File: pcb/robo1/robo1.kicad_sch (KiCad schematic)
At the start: 9 parts, among them J1 Conn_02x05_Odd_Even, J2 Conn_02x05_Odd_Even, J3 Conn_01x05_Pin, J4 Conn_01x05_Pin, U1 Pico

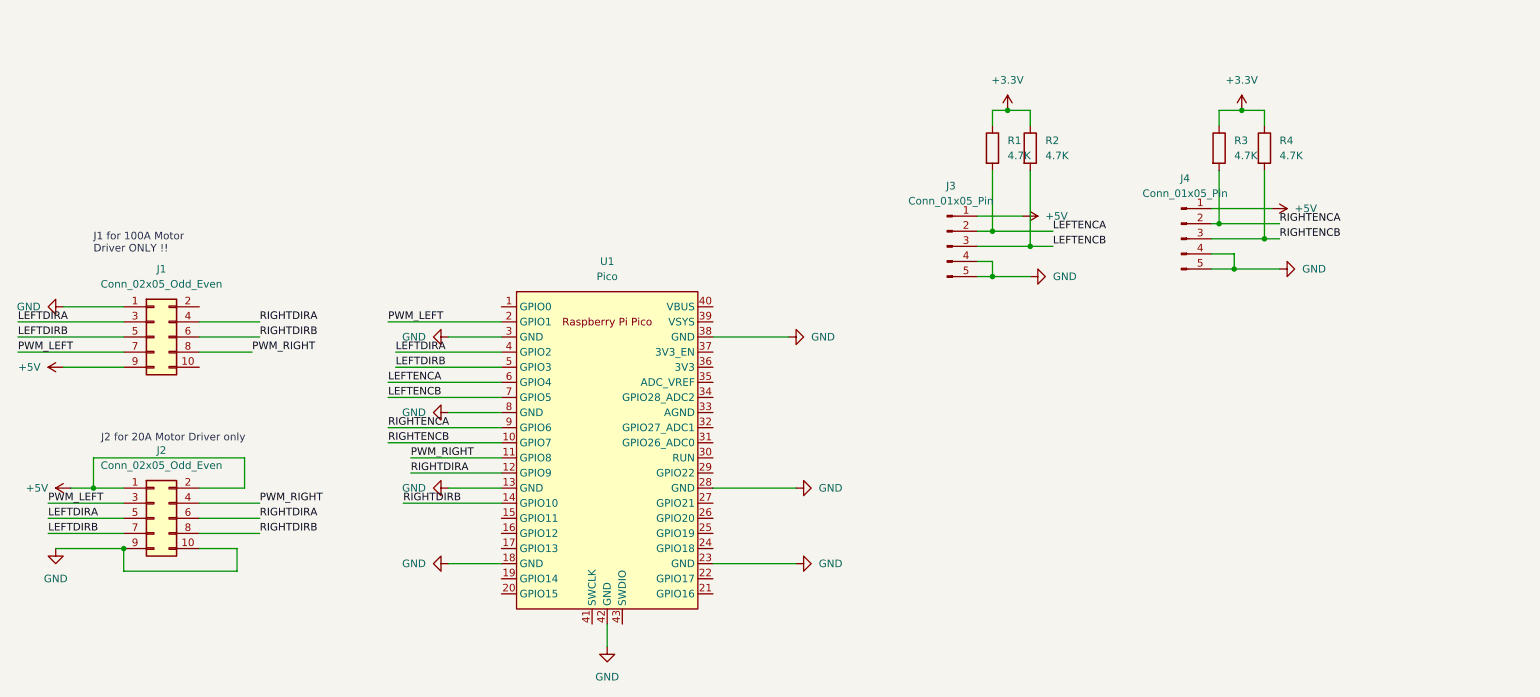
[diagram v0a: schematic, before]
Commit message: Add OLED to PCB
OLED added to pcb
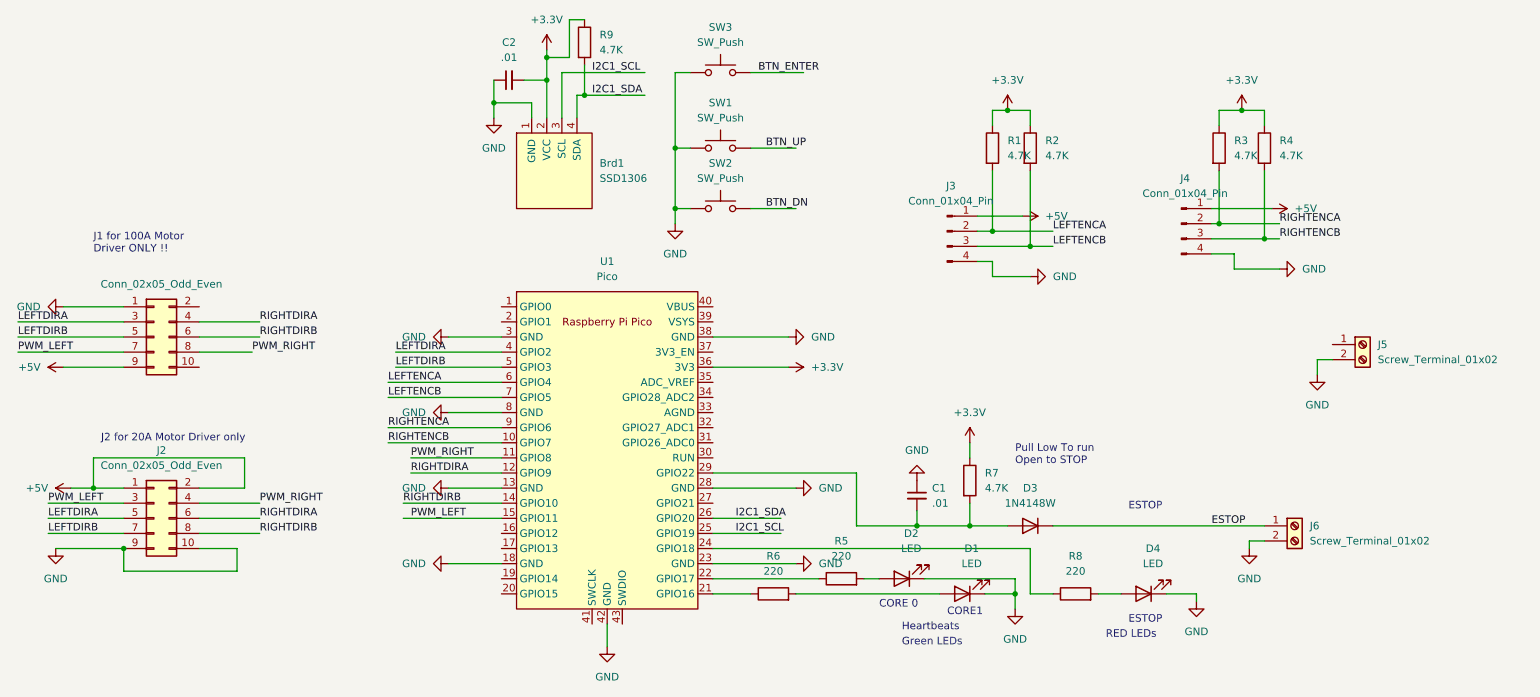
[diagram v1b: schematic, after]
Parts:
- removed J3, J4: Conn_01x05_Pin, Connector_PinHeader_2.54mm:PinHeader_1x05_P2.54mm_Vertical, symbol Connector:Conn_01x05_Pin
- added Brd1: SSD1306, SSD1306:128x64OLED, symbol SSD1306-128x64_OLED:SSD1306
- added C1, C2: .01, Capacitor_SMD:C_0603_1608Metric_Pad1.08x0.95mm_HandSolder, symbol Device:C_Small
- added D1, D2, D4: LED, LED_SMD:LED_1206_3216Metric_Pad1.42x1.75mm_HandSolder, symbol Device:LED
- added D3: 1N4148W, Diode_SMD:D_SOD-123, symbol Diode:1N4148W
- added J3, J4: Conn_01x04_Pin, Connector_PinHeader_2.54mm:PinHeader_1x04_P2.54mm_Vertical, symbol Connector:Conn_01x04_Pin
- added J5, J6: Screw_Terminal_01x02, TerminalBlock:TerminalBlock_bornier-2_P5.08mm, symbol Connector:Screw_Terminal_01x02
- added R5, R6, R8: 220, Resistor_SMD:R_0201_0603Metric_Pad0.64x0.40mm_HandSolder, symbol Device:R
- added R7, R9: 4.7K, Resistor_SMD:R_0201_0603Metric_Pad0.64x0.40mm_HandSolder, symbol Device:R
- added SW1, SW2, SW3: SW_Push, Button_Switch_THT:SW_PUSH_6mm, symbol Switch:SW_Push
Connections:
- net +3.3V: now also U1.36 (3V3), Brd1.2 (VCC), C2.2, R7.1, R9.1
- net +5V: now also J3.1 (Pin_1), J4.1 (Pin_1)
- net GND: now also Brd1.1 (GND), C1.1, C2.1, D1.1 (K), D2.1 (K), D4.1 (K), J3.4 (Pin_4), J4.4 (Pin_4), J5.2 (Pin_2), J6.2 (Pin_2), SW1.1, SW2.1, SW3.1
- net LEFTENCA: now also J3.2 (Pin_2)
- net LEFTENCB: now also J3.3 (Pin_3)
- net PWM_LEFT: now also U1.15 (GPIO11); no longer U1.2 (GPIO1)
- net RIGHTENCA: now also J4.2 (Pin_2)
- net RIGHTENCB: now also J4.3 (Pin_3)
- net at U1.21 (GPIO16): now also R6.1
- net at U1.22 (GPIO17): now also R5.1
- net at U1.24 (GPIO18): now also R8.1
- net I2C1_SCL: now reaches U1.25 (GPIO19)
- net I2C1_SCL: now also Brd1.3 (SCL)
- net I2C1_SDA: now reaches U1.26 (GPIO20)
- net I2C1_SDA: now also Brd1.4 (SDA), R9.2
- net at U1.29 (GPIO22): now also C1.2, D3.2 (A), R7.2
- new net: D4.2 (A), R8.2
- new net: D2.2 (A), R5.2
- new net: D1.2 (A), R6.2
- new net BTN_DN: SW2.2
- new net BTN_ENTER: SW3.2
- new net BTN_UP: SW1.2
- new net ESTOP: D3.1 (K), J6.1 (Pin_1)
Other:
- note added: "CORE 0"
- note added: "CORE1"
- note added: "ESTOP"
- note added: "Green LEDs"
- note added: "Heartbeats"
- note added: "Pull Low To run Open to STOP"
- note added: "RED LEDs"

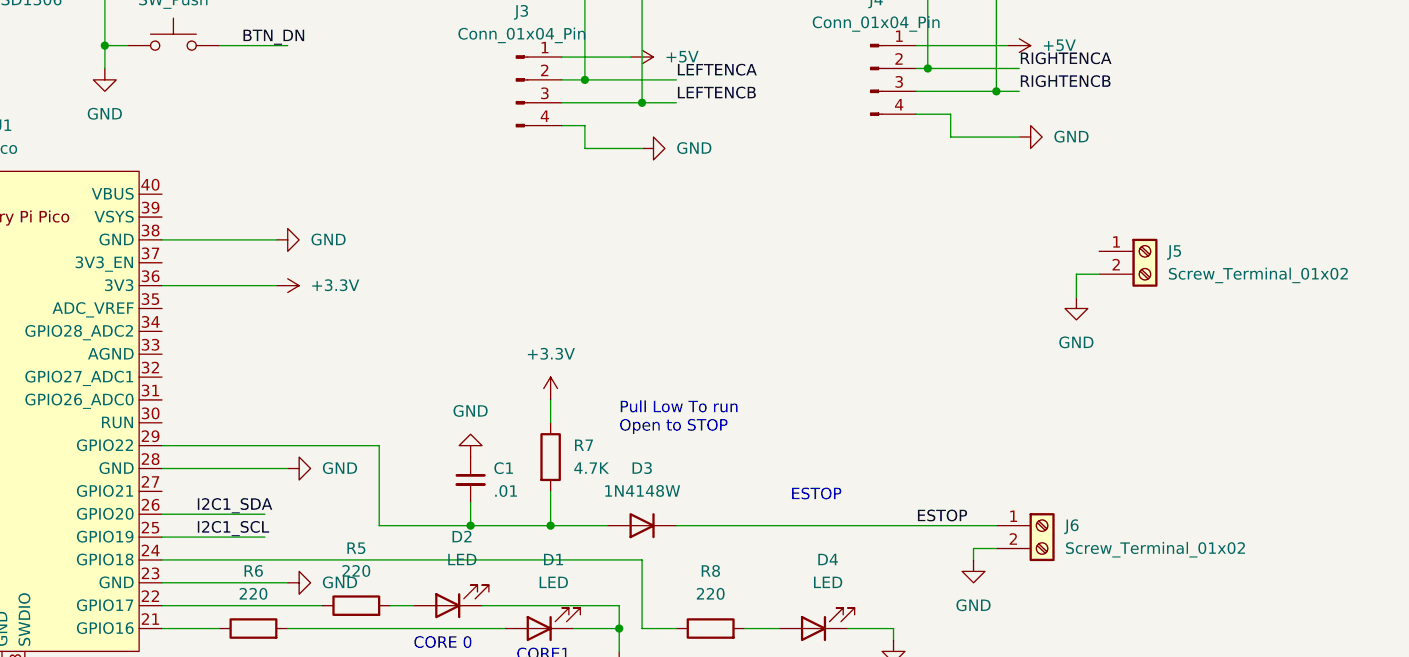
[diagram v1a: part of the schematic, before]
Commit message: PCB added Isense connectors
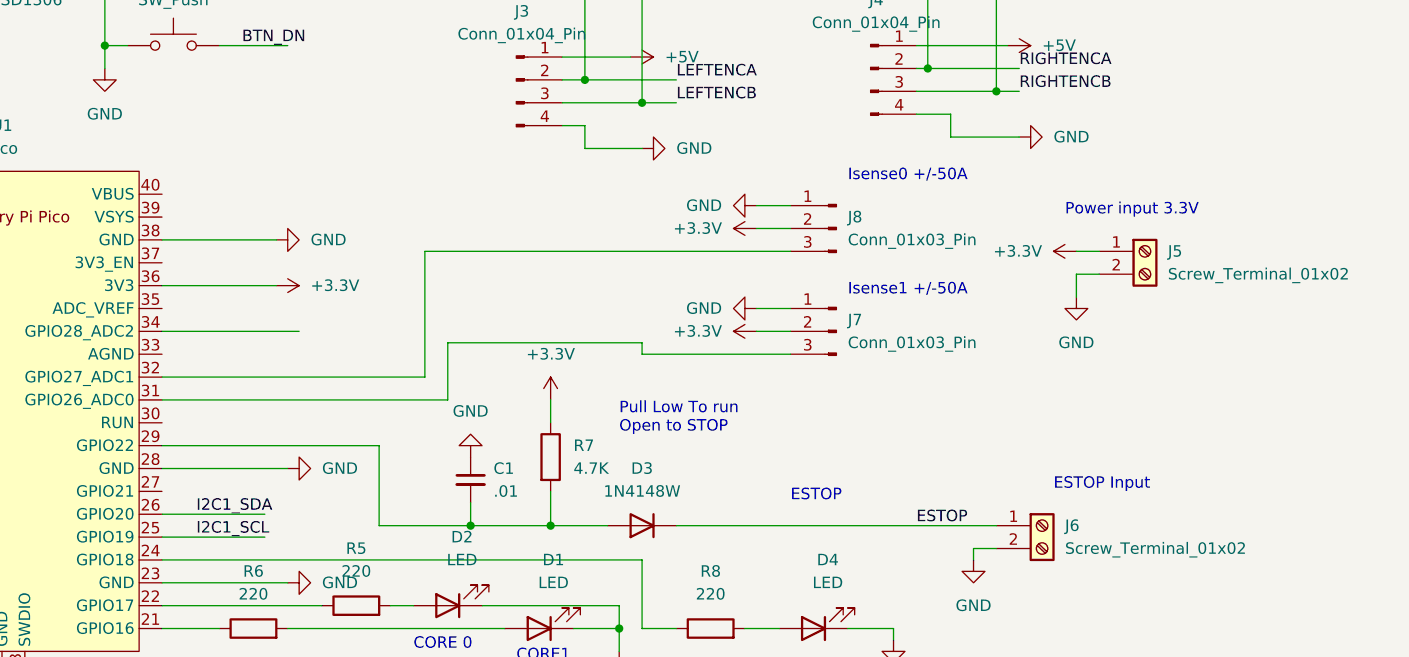
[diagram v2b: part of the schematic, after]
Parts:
- added J7, J8: Conn_01x03_Pin, Connector_PinHeader_2.54mm:PinHeader_1x03_P2.54mm_Vertical, symbol Connector:Conn_01x03_Pin
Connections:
- net +3.3V: now also J5.1 (Pin_1), J7.2 (Pin_2), J8.2 (Pin_2)
- net GND: now also J7.1 (Pin_1), J8.1 (Pin_1)
- net at U1.31 (GPIO26_ADC0): now also J7.3 (Pin_3)
- net at U1.32 (GPIO27_ADC1): now also J8.3 (Pin_3)
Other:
- note added: "ESTOP Input"
- note added: "Isense0 +/-50A"
- note added: "Isense1 +/-50A"
- note added: "Power input 3.3V"

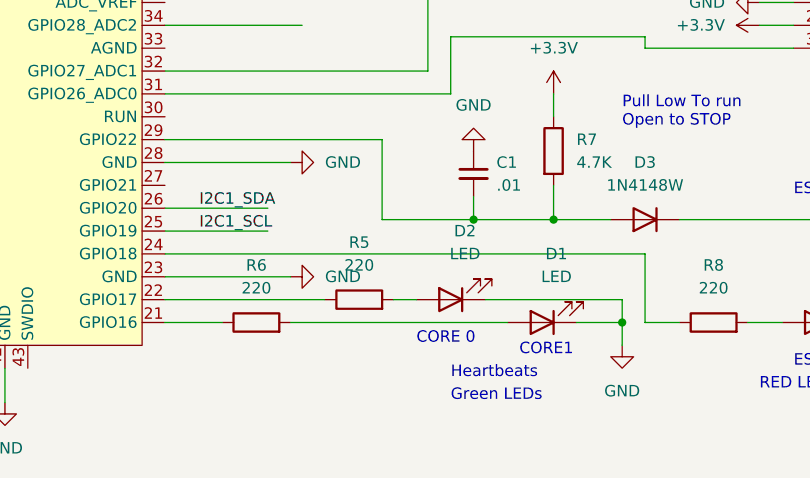
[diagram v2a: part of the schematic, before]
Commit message: add oled
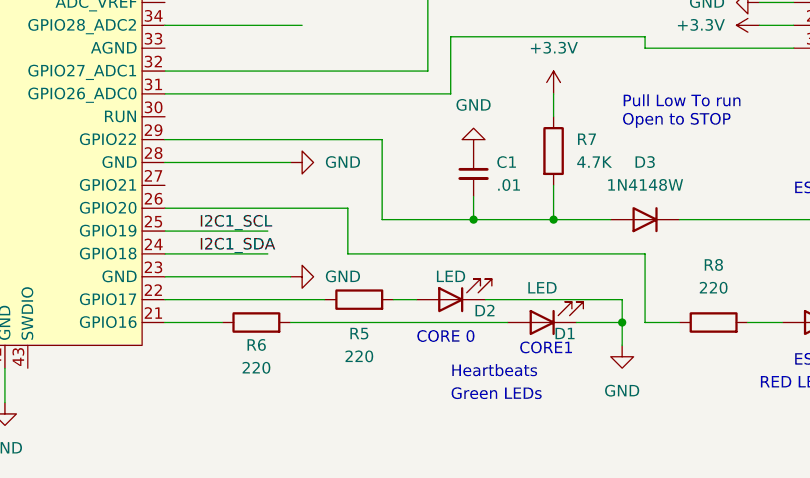
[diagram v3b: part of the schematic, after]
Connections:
- net I2C1_SDA: now also U1.24 (GPIO18); no longer U1.26 (GPIO20)
- net at R8.1: now also U1.26 (GPIO20); no longer U1.24 (GPIO18)
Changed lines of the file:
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@@
+    (stroke (width 0) (type default))
+  )
+  (wire (pts (xy 166.37 97.79) (xy 186.69 97.79))
     (stroke (width 0) (type default))
   )
@@
     (stroke (width 0) (type default))
   )
+  (wire (pts (xy 186.69 102.87) (xy 219.71 102.87))
+    (stroke (width 0) (type default))
+  )
   (wire (pts (xy 80.01 64.77) (xy 90.17 64.77))
     (stroke (width 0) (type default))
@@
     (stroke (width 0) (type default))
   )
-  (wire (pts (xy 166.37 97.79) (xy 177.8 97.79))
-    (stroke (width 0) (type default))
-  )
   (wire (pts (xy 166.37 82.55) (xy 195.58 82.55))
     (stroke (width 0) (type default))
@@
     (stroke (width 0) (type default))
   )
+  (wire (pts (xy 186.69 97.79) (xy 186.69 102.87))
+    (stroke (width 0) (type default))
+  )
   (wire (pts (xy 129.54 24.13) (xy 129.54 27.94))
     (stroke (width 0) (type default))
@@
     (stroke (width 0) (type default))
   )
-  (wire (pts (xy 166.37 102.87) (xy 219.71 102.87))
+  (wire (pts (xy 166.37 102.87) (xy 177.8 102.87))
     (stroke (width 0) (type default))
   )
@@
     (effects (font (size 1.27 1.27)) (justify left bottom))
   )
-  (label "I2C1_SDA" (at 170.18 97.79 0) (fields_autoplaced)
+  (label "I2C1_SDA" (at 170.18 102.87 0) (fields_autoplaced)
     (effects (font (size 1.27 1.27)) (justify left bottom))
   )
@@
   )
   (symbol (lib_id "Device:R") (at 187.96 107.95 90) (unit 1)
-    (in_bom yes) (on_board yes) (dnp no) (fields_autoplaced)
-    (property "Reference" "R5" (at 187.96 101.6 90)
-      (effects (font (size 1.27 1.27)))
-    )
-    (property "Value" "220" (at 187.96 104.14 90)
+    (in_bom yes) (on_board yes) (dnp no)
+    (property "Reference" "R5" (at 187.96 111.76 90)
+      (effects (font (size 1.27 1.27)))
+    )
+    (property "Value" "220" (at 187.96 114.3 90)
       (effects (font (size 1.27 1.27)))
     )
@@
   )
   (symbol (lib_id "Device:LED") (at 208.28 110.49 180) (unit 1)
-    (in_bom yes) (on_board yes) (dnp no) (fields_autoplaced)
-    (property "Reference" "D1" (at 209.8675 102.87 0)
-      (effects (font (size 1.27 1.27)))
-    )
-    (property "Value" "LED" (at 209.8675 105.41 0)
+    (in_bom yes) (on_board yes) (dnp no)
+    (property "Reference" "D1" (at 210.82 111.76 0)
+      (effects (font (size 1.27 1.27)))
+    )
+    (property "Value" "LED" (at 208.28 106.68 0)
       (effects (font (size 1.27 1.27)))
     )
@@
   )
   (symbol (lib_id "Device:R") (at 176.53 110.49 90) (unit 1)
-    (in_bom yes) (on_board yes) (dnp no) (fields_autoplaced)
-    (property "Reference" "R6" (at 176.53 104.14 90)
-      (effects (font (size 1.27 1.27)))
-    )
-    (property "Value" "220" (at 176.53 106.68 90)
+    (in_bom yes) (on_board yes) (dnp no)
+    (property "Reference" "R6" (at 176.53 113.03 90)
+      (effects (font (size 1.27 1.27)))
+    )
+    (property "Value" "220" (at 176.53 115.57 90)
       (effects (font (size 1.27 1.27)))
     )
@@
   )
   (symbol (lib_id "Device:LED") (at 198.12 107.95 180) (unit 1)
-    (in_bom yes) (on_board yes) (dnp no) (fields_autoplaced)
-    (property "Reference" "D2" (at 199.7075 100.33 0)
-      (effects (font (size 1.27 1.27)))
-    )
-    (property "Value" "LED" (at 199.7075 102.87 0)
-      (effects (font (size 1.27 1.27)))
-    )
+    (in_bom yes) (on_board yes) (dnp no)
+    (property "Reference" "D2" (at 201.93 109.22 0)
+      (effects (font (size 1.27 1.27)))
+    )
+    (property "Value" "LED" (at 198.12 105.41 0)
+      (effects (font (size 1.27 1.27)))
+    )
